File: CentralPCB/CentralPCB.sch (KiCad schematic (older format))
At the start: 60 parts, among them J1 POWER HEADER, J2 SPI Header, J3 Conn_01x24, J4 Conn_01x24, J5 Conn_02x16_Odd_Even, J6 Conn_Coaxial, J7 Conn_02x10_Odd_Even, J8 Conn_01x05, U1 AD8531, U2 Teensy4.1, U3 BA7810CP-E2

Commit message: Revert "Sav"
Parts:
- removed D1: 12V_POW, LED_THT:LED_D3.0mm, symbol Device:LED
- removed J3, J4: Conn_01x24, Connector_PinSocket_2.54mm:PinSocket_1x24_P2.54mm_Vertical, symbol Connector_Generic:Conn_01x24
- removed J5: Conn_02x16_Odd_Even, Connector_PinSocket_2.54mm:PinSocket_2x16_P2.54mm_Vertical, symbol Connector_Generic:Conn_02x16_Odd_Even
- removed J6: Conn_Coaxial, Connector_Coaxial:SMB_Jack_Vertical, symbol Connector:Conn_Coaxial
- removed J7: Conn_02x10_Odd_Even, Connector_PinSocket_2.54mm:PinSocket_2x10_P2.54mm_Vertical, symbol Connector_Generic:Conn_02x10_Odd_Even
- removed J8: Conn_01x05, Connectors_Phoenix:PhoenixContact_GMSTBVA-G_05x7.50mm_Vertical, symbol Connector_Generic:Conn_01x05
- removed R1: ?, Resistor_SMD:R_0805_2012Metric, symbol Device:R_US
- removed R10, R11, R12, R13, R14, R15, R16, R17, R18, R19, R20, R21, R22, R23, R8, R9: 200, Resistor_SMD:R_0805_2012Metric, symbol Device:R_US
- removed U1: AD8531, Package_SO:SOIC-8_3.9x4.9mm_P1.27mm, symbol Amplifier_Operational:OP179GS
- removed U2: Teensy4.1, teensy:Teensy41, symbol teensy:Teensy4.1
- added J5: MIDI IN, Connector_PinSocket_2.54mm:PinSocket_1x03_P2.54mm_Vertical, symbol Connector_Generic:Conn_01x03
- added J6: MIDI OUT, Connector_PinSocket_2.54mm:PinSocket_1x03_P2.54mm_Vertical, symbol Connector_Generic:Conn_01x03
- added J?: Conn_02x16_Top_Bottom, Connector_PinSocket_2.54mm:PinSocket_2x16_P2.54mm_Vertical, symbol Connector_Generic:Conn_02x16_Top_Bottom
- added J?: Conn_01x05, symbol Connector_Generic:Conn_01x05
- added U1: Teensy4.1, symbol teensy:Teensy4.1
- J4: renamed from J2; value SPI Header -> SPI Header 1
- renumbered D4 to D1, D5 to D19, D3 to D20, D6 to D21, D7 to D22, D2 to D5, D9 to D?, D10 to D?, D11 to D?, D12 to D?, D13 to D?, D14 to D?, D15 to D?, D16 to D?, D17 to D?, D18 to D?, D19 to D?, D20 to D?, D21 to D?, D22 to D?, D23 to D?, D8 to D?, R2 to R33, R3 to R34, R4 to R35, R5 to R36, R6 to R37, R7 to R38, U3 to U2
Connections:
- net labels added: CS1, MISO1, MOSI1, SCK1
- net labels removed: CLR, LDAC, RESET, SCL, SDA
- wire segments 309 -> 218
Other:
- moved on the sheet: D1, D19, D20, D21, D22, D5, D?, J1, J4, R33, R34, R35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

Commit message: Squashed commit of the following:
commit 4cc6f9daa43c8e58e4c19e3ea2c52996bd638c5b
Author: SavHearn <sav.hearn@gmail.com>
Date:   Tue Oct 26 14:19:17 2021 -0400

    Auto generated file
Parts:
- removed D5: 5V_POW, LED_THT:LED_D3.0mm, symbol Device:LED
- removed D? (x16): 3.3v Zener, Diode_SMD:D_SOD-123, symbol Diode:BZT52Bxx
- removed TH1, TH2, TH3: Thermistor_US, Resistor_SMD:R_1206_3216Metric, symbol Device:Thermistor_US
- added D10, D11, D12, D13, D14, D15, D16, D17, D18, D19, D20, D21, D22, D23, D8, D9, D? (x16): 3.3v Zener, Diode_SMD:D_SOD-123, symbol Diode:BZT52Bxx
- added D2, D5: 5V_POW, LED_THT:LED_D3.0mm, symbol Device:LED
- added D3: 12V_POW, LED_THT:LED_D3.0mm, symbol Device:LED
- added D5, D6, D7: POW, LED_THT:LED_D3.0mm, symbol Device:LED
- added J2: SPI Header, Connector_PinSocket_2.54mm:PinSocket_1x04_P2.54mm_Vertical, symbol Connector_Generic:Conn_01x04
- added J5: Conn_02x16_Odd_Even, Connector_PinSocket_2.54mm:PinSocket_2x16_P2.54mm_Vertical, symbol Connector_Generic:Conn_02x16_Odd_Even
- added R10, R11, R12, R13, R14, R15, R16, R17, R18, R19, R20, R21, R22, R23, R8, R9: 200, Resistor_SMD:R_0805_2012Metric, symbol Device:R_US
- added R2, R3, R4, R5, R6, R7: ?, Resistor_SMD:R_0805_2012Metric, symbol Device:R_US
- added TH1 (x2), TH2 (x2), TH3 (x2): Thermistor_US, Resistor_SMD:R_1206_3216Metric, symbol Device:Thermistor_US
- added U1: AD8531, Package_SO:SOIC-8_3.9x4.9mm_P1.27mm, symbol Amplifier_Operational:OP179GS
- added U3: BA7810CP-E2, Package_TO_SOT_THT:TO-220-3_Vertical, symbol CentralPCB-rescue:BA7810CP-E2-test-lib
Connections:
- wire segments 218 -> 312
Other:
- moved on the sheet: D10, D11, D12, D13, D14, D15, D16, D17, D18, D19, D2, D20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

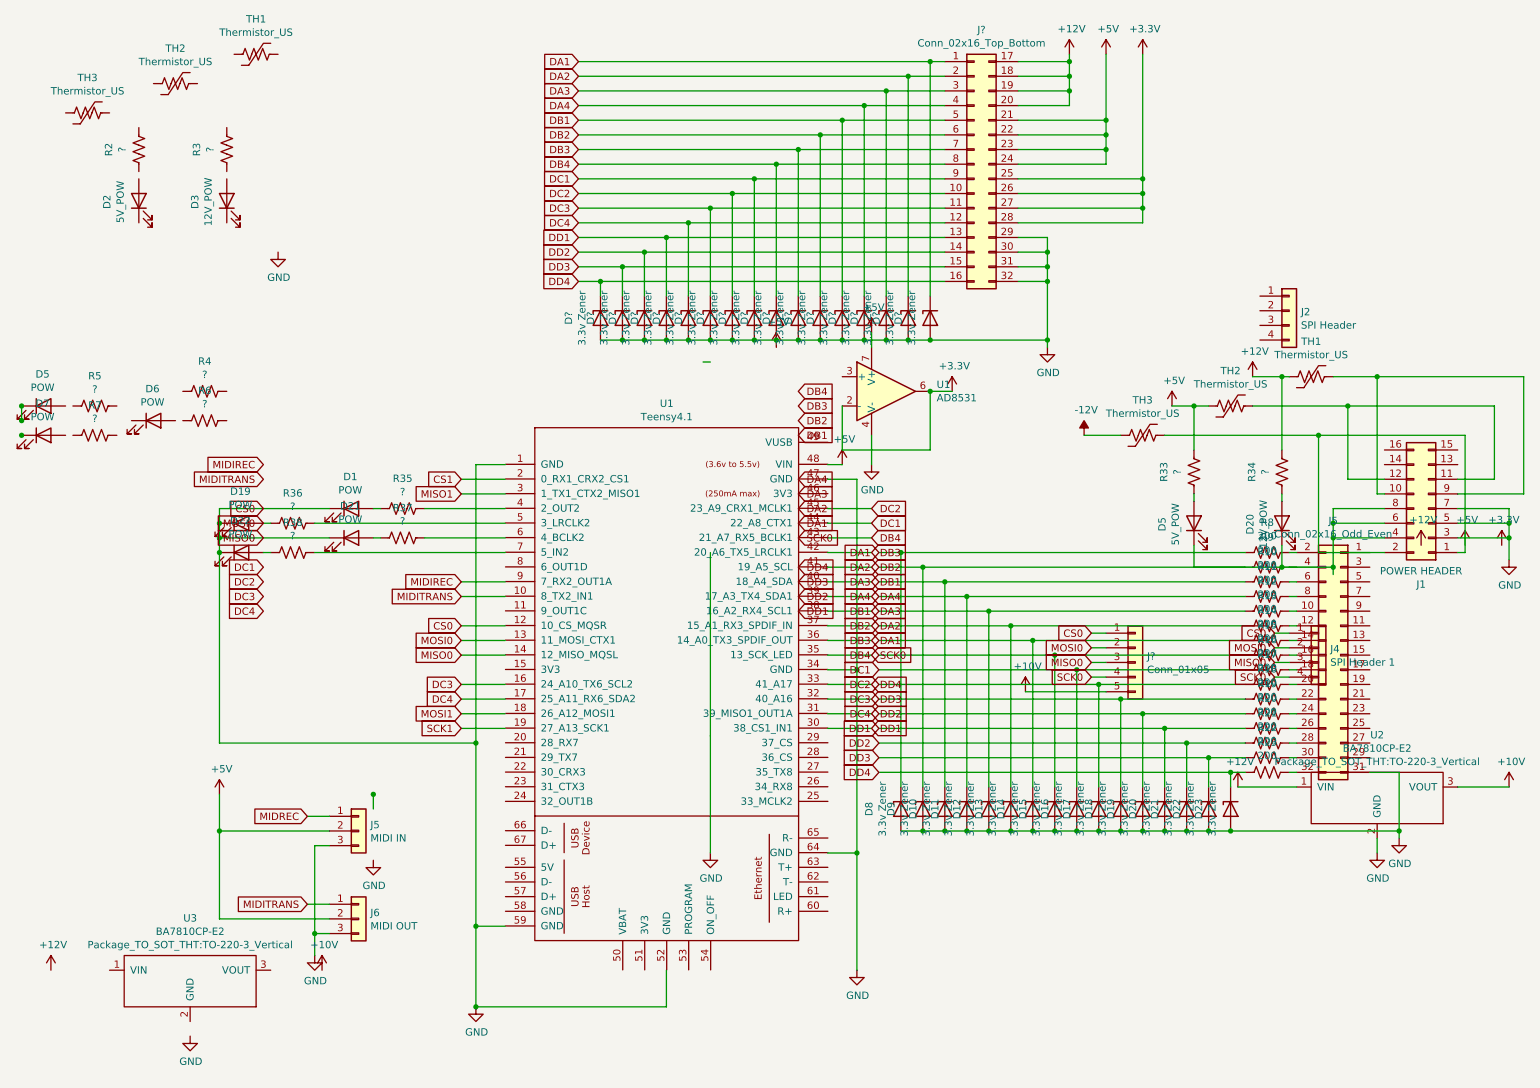
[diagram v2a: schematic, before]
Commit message: Fixed glitched CentralPCB schematic
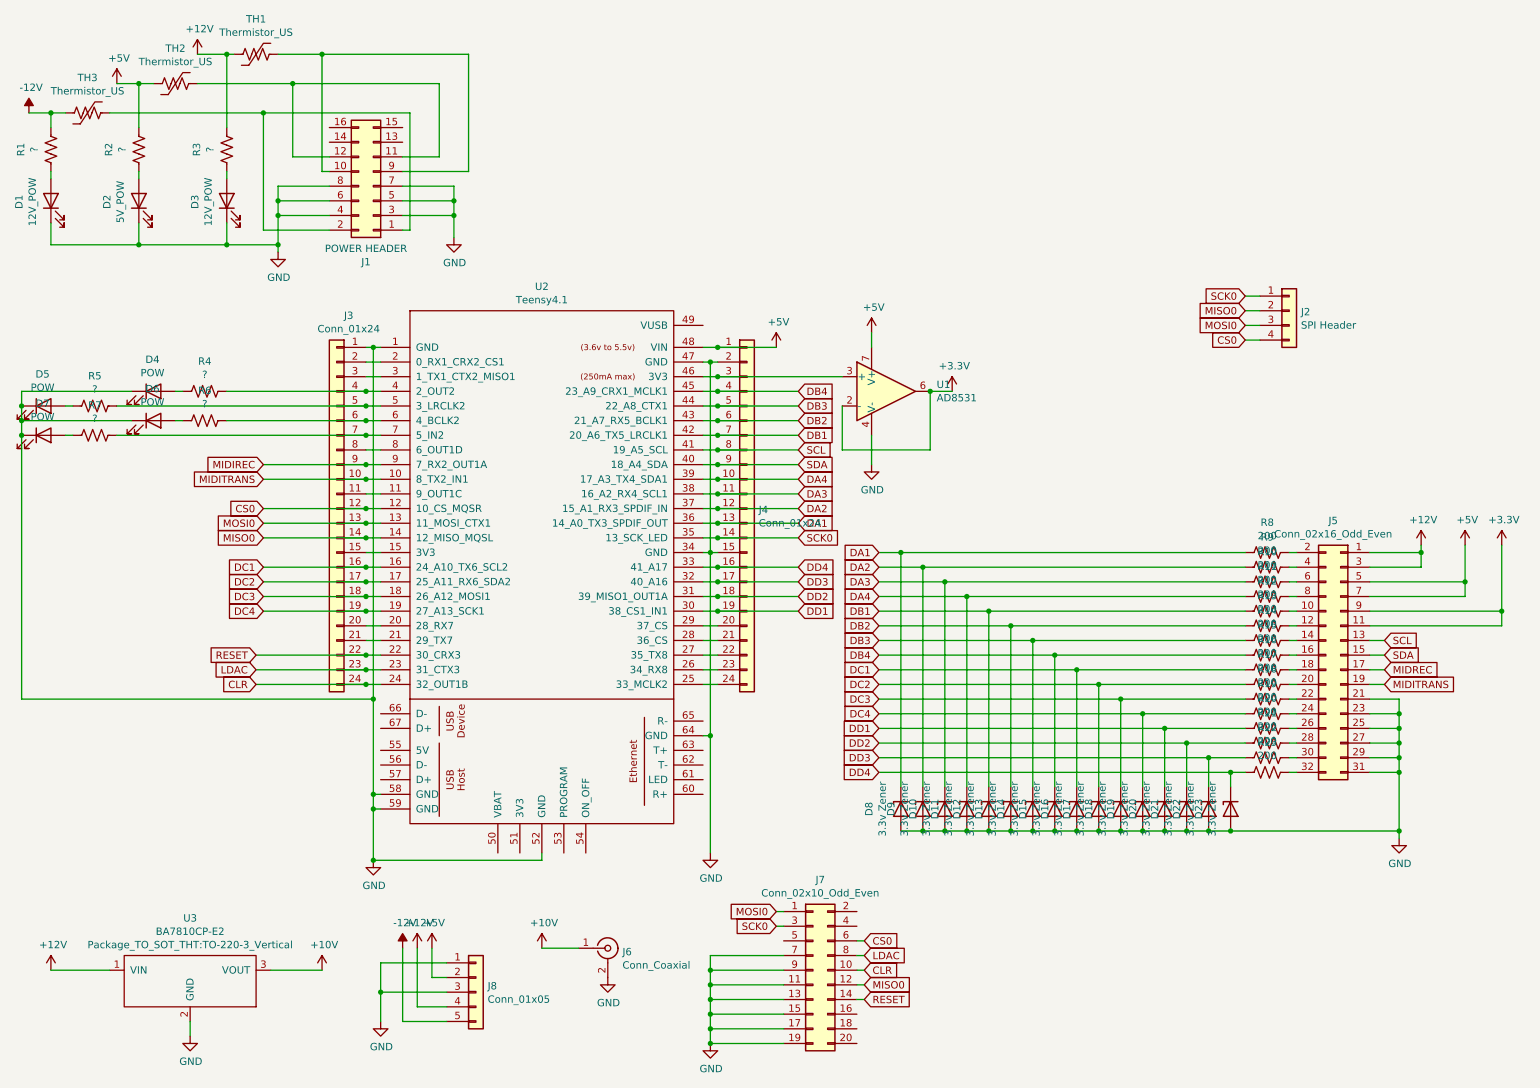
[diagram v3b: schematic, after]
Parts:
- removed D19, D21, D22, D5: POW, LED_THT:LED_D3.0mm, symbol Device:LED
- removed D20: 12V_POW, LED_THT:LED_D3.0mm, symbol Device:LED
- removed D5: 5V_POW, LED_THT:LED_D3.0mm, symbol Device:LED
- removed D? (x16): 3.3v Zener, Diode_SMD:D_SOD-123, symbol Diode:BZT52Bxx
- removed J4: SPI Header 1, Connector_PinSocket_2.54mm:PinSocket_1x04_P2.54mm_Vertical, symbol Connector_Generic:Conn_01x04
- removed J5: MIDI IN, Connector_PinSocket_2.54mm:PinSocket_1x03_P2.54mm_Vertical, symbol Connector_Generic:Conn_01x03
- removed J6: MIDI OUT, Connector_PinSocket_2.54mm:PinSocket_1x03_P2.54mm_Vertical, symbol Connector_Generic:Conn_01x03
- removed J?: Conn_02x16_Top_Bottom, Connector_PinSocket_2.54mm:PinSocket_2x16_P2.54mm_Vertical, symbol Connector_Generic:Conn_02x16_Top_Bottom
- removed J?: Conn_01x05, symbol Connector_Generic:Conn_01x05
- removed R33, R34, R35, R36, R37, R38: ?, Resistor_SMD:R_0805_2012Metric, symbol Device:R_US
- removed TH1 (x2), TH2 (x2), TH3 (x2): Thermistor_US, Resistor_SMD:R_1206_3216Metric, symbol Device:Thermistor_US
- removed U1: Teensy4.1, symbol teensy:Teensy4.1
- removed U2: BA7810CP-E2, Package_TO_SOT_THT:TO-220-3_Vertical, symbol test-lib:BA7810CP-E2
- added D1: 12V_POW, LED_THT:LED_D3.0mm, symbol Device:LED
- added D5: POW, LED_THT:LED_D3.0mm, symbol Device:LED
- added J3, J4: Conn_01x24, Connector_PinSocket_2.54mm:PinSocket_1x24_P2.54mm_Vertical, symbol Connector_Generic:Conn_01x24
- added J6: Conn_Coaxial, Connector_Coaxial:SMB_Jack_Vertical, symbol Connector:Conn_Coaxial
- added J7: Conn_02x10_Odd_Even, Connector_PinSocket_2.54mm:PinSocket_2x10_P2.54mm_Vertical, symbol Connector_Generic:Conn_02x10_Odd_Even
- added J8: Conn_01x05, Connectors_Phoenix:PhoenixContact_GMSTBVA-G_05x7.50mm_Vertical, symbol Connector_Generic:Conn_01x05
- added R1: ?, Resistor_SMD:R_0805_2012Metric, symbol Device:R_US
- added TH1, TH2, TH3: Thermistor_US, Resistor_SMD:R_1206_3216Metric, symbol Device:Thermistor_US
- added U2: Teensy4.1, teensy:Teensy41, symbol teensy:Teensy4.1
- renumbered D1 to D4
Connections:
- net labels added: CLR, LDAC, RESET, SCL, SDA
- net labels removed: CS1, MISO1, MOSI1, SCK1
- wire segments 312 -> 309
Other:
- moved on the sheet: D4, J1
